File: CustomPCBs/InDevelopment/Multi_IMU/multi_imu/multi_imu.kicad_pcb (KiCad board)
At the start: 4 copper layers, 7.3 x 12.7 mm, 8 parts, among them J3 Conn_01x04_MountingPin, J4 Conn_01x04_MountingPin, U1 LSM6DSV

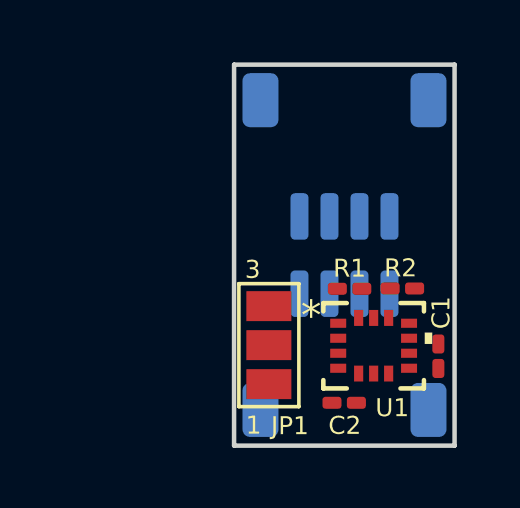
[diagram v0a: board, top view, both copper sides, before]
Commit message: Adding mags to lsm/bmi chips
Going to use one or the other, depending whether lsm or bmi is used
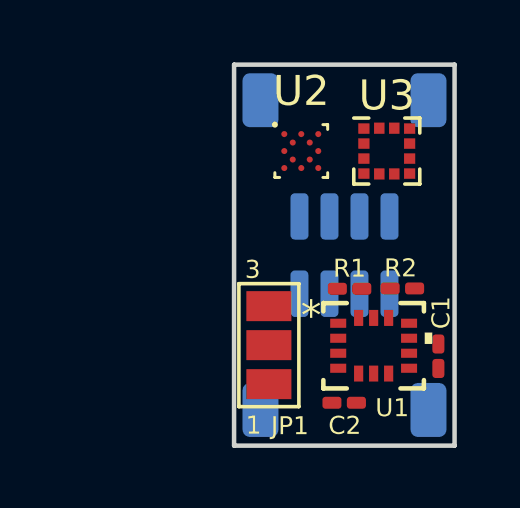
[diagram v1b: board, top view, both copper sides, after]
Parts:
- added U2: BMM150, Package_CSP:WLCSP-12_1.56x1.56mm_P0.4mm, F.Cu at (158.9, 126.6)
- added U3: LIS2MDL, Package_LGA:LGA-12_2x2mm_P0.5mm, F.Cu at (161.8, 126.6)

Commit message: Finished ICM-20948 board
DRC is OK
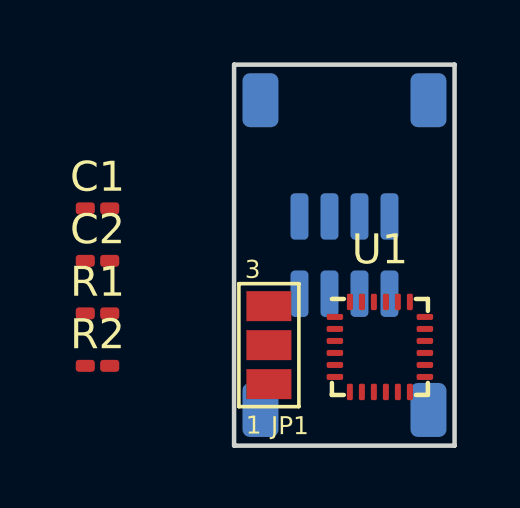
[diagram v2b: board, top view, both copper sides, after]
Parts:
- removed U2: BMM150, Package_CSP:WLCSP-12_1.56x1.56mm_P0.4mm
- removed U3: LIS2MDL, Package_LGA:LGA-12_2x2mm_P0.5mm
- U1: value LSM6DSV -> ICM-20948; footprint footprints:LGA14-L_2P59X3P1X0P5_STM -> Sensor_Motion:InvenSense_QFN-24_3x3mm_P0.4mm
- moved C1 12.4 mm to (152.2, 128.6), turned to 0 degrees
- moved R2 10.5 mm to (152.2, 133.8), turned to 0 degrees
- moved C2 9.49 mm to (152.2, 130.3), turned to 0 degrees
- moved R1 8.44 mm to (152.2, 132.1)
- moved U1 0.21 mm to (161.6, 133.2)
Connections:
- U1 pad 1: Net-(JP1-C) -> unconnected-(U1-NC-Pad1)
- U1 pad 13: SCL -> unconnected-(U1-VDD-Pad13)
- U1 pad 14: SDA -> unconnected-(U1-NC-Pad14)
- U1 pad 5: +3.3V -> unconnected-(U1-NC-Pad5)
- U1 pad 6: GND -> unconnected-(U1-NC-Pad6)
- U1 pad 7: GND -> unconnected-(U1-AUX_CL-Pad7)
- U1 pad 8: +3.3V -> unconnected-(U1-VDDIO-Pad8)
- U1 pad 9: unconnected-(U1-INT2-Pad9) -> Net-(JP1-C)
